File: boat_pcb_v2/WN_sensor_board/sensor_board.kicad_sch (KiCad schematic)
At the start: 117 parts, among them J1 MSD-4-A, J10 PPTC031LFBN-RC, J11 RFPC-SMA28-F, J12 PPTC031LFBN-RC, J13 PPTC031LFBN-RC, J14 RFPC-SMA28-F, J15 USB4120-03-C_REVA6, J16 USB4120-03-C_REVA6, J17 PPTC031LFBN-RC, J18 PPTC031LFBN-RC, J2 RFPC-SMA28-F, J20 TSW-108-07-F-D, J21 TSW-108-07-F-D, J22 TSW-108-07-F-D, J3 RFPC-SMA28-F, J4 RFPC-SMA28-F, J5 PPTC031LFBN-RC, J6 PPTC031LFBN-RC, J7 PPTC031LFBN-RC, J8 PPTC031LFBN-RC, J9 PPTC031LFBN-RC, U1 MAX14933ASE_T, U16 BSS123-7-F, U17 BSS123-7-F, U18 BSS123-7-F, U19 BSS123-7-F, U2 ESP32-S3-WROOM-1-N8, U3 MCP2200-I_SO, U4 AP62301WU-7, U5 MAX14933ASE_T, U6 MAX14933ASE_T, U7 MAX14933ASE_T, U8 BSS123-7-F, U9 BSS123-7-F, Y1 ECS-120-12-33-AGN-TR

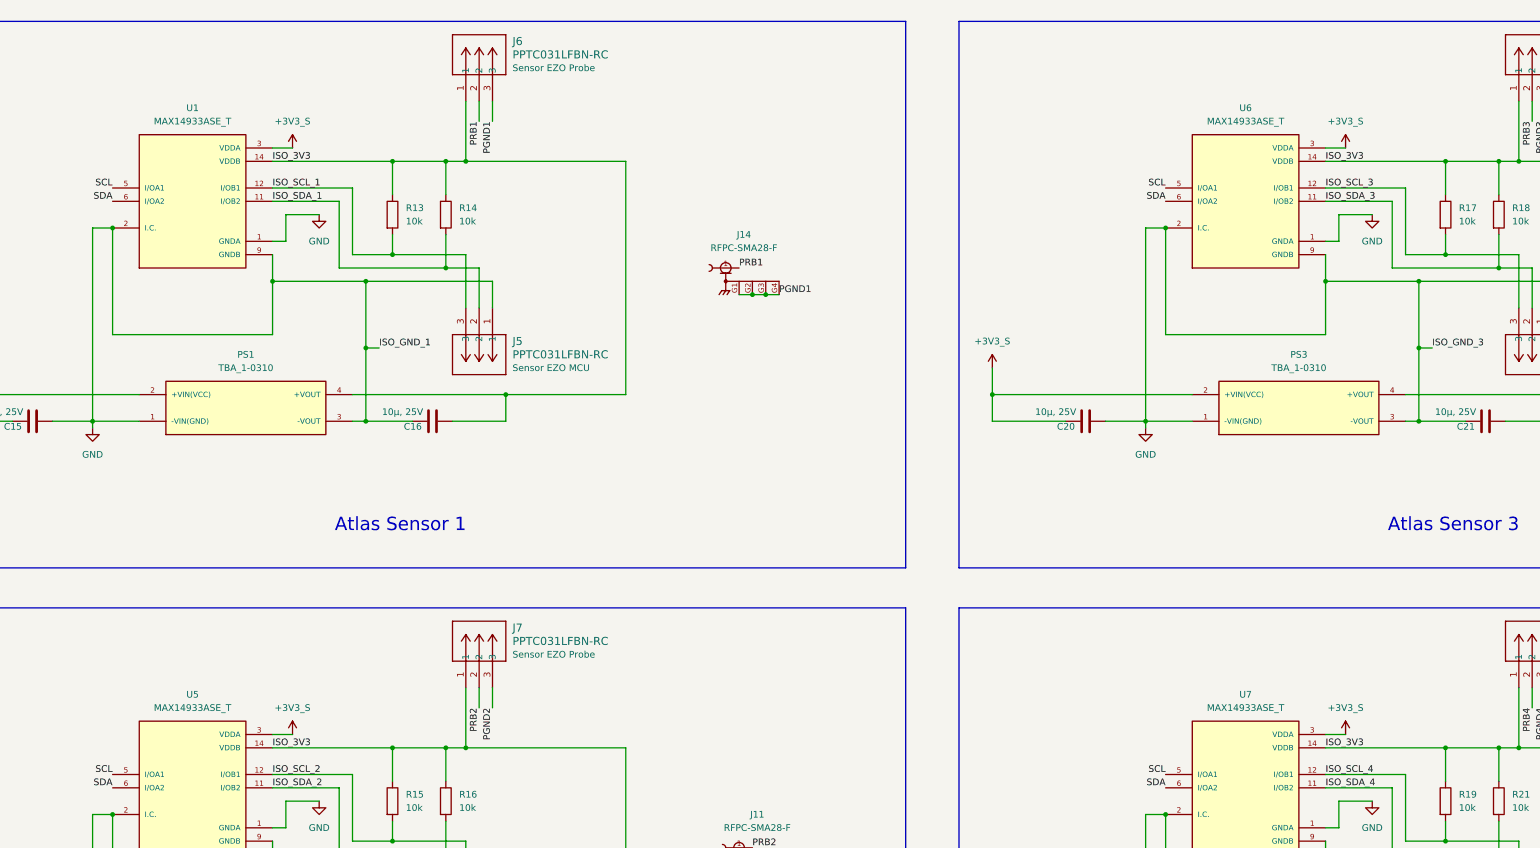
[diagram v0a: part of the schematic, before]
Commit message: fixed some footprints
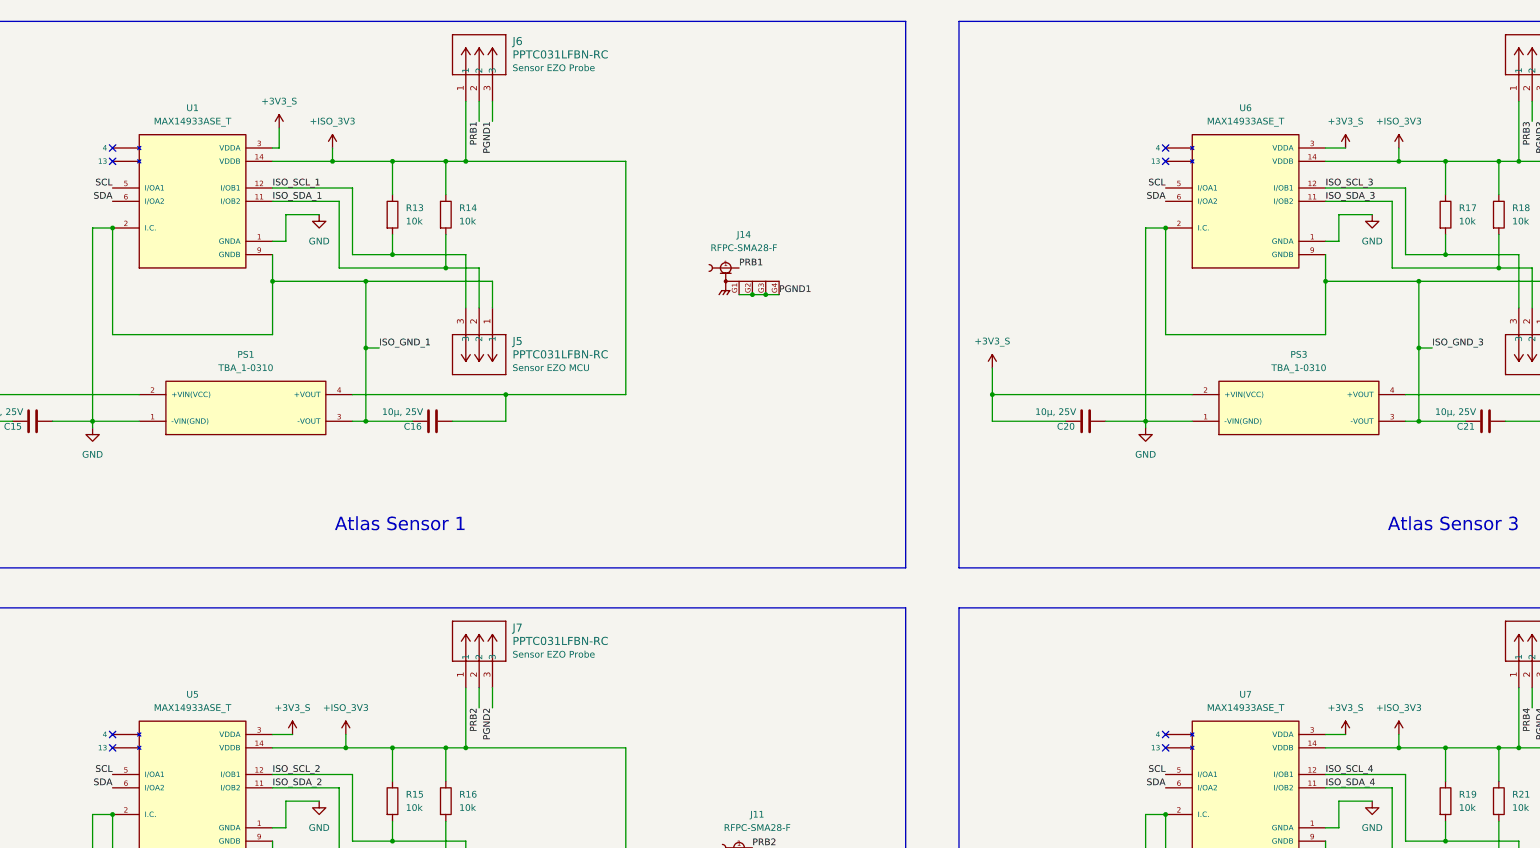
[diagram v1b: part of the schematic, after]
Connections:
- net ISO_3V3 renamed +ISO_3V3
- no-connect marks 17 -> 25

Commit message: minor updates related to board layout
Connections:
- net +3V3: now also J22.12, J22.14, J22.16
- net COVER_GND: now also J22.15
- net IO1: now also J22.01
- net IO2: now also J22.03
- net IO17: now reaches U2.10 (IO17)
- net IO17: now also J22.11
- net IO18: now reaches U2.11 (IO18)
- net IO18: now also J22.13
- net IO3: now reaches U2.15 (IO3)
- net IO3: now also J22.05
- net IO47: now reaches U2.24 (IO47)
- net IO47: now also J22.08
- net IO48: now reaches U2.25 (IO48)
- net IO48: now also J22.10
- net IO40: now reaches U2.33 (IO40)
- net IO40: now also J22.02
- net IO41: now reaches U2.34 (IO41)
- net IO41: now also J22.04
- net IO42: now reaches U2.35 (IO42)
- net IO42: now also J22.06
- net IO6: now reaches U2.6 (IO6)
- net IO6: now also J22.07
- net IO7: now reaches U2.7 (IO7)
- net IO7: now also J22.09
- no-connect marks 25 -> 17
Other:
- moved on the sheet: J22
